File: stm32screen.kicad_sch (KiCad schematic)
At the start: 31 parts, among them J1 SWD, J2 GC9A01, J3 Oil temp sensor, J4 pressure sensor, J5 POWER IN, SW1 SW_Push, SW2 SW_Push, U1 TS1117BCW-3.3, U2 STM32F407VETx

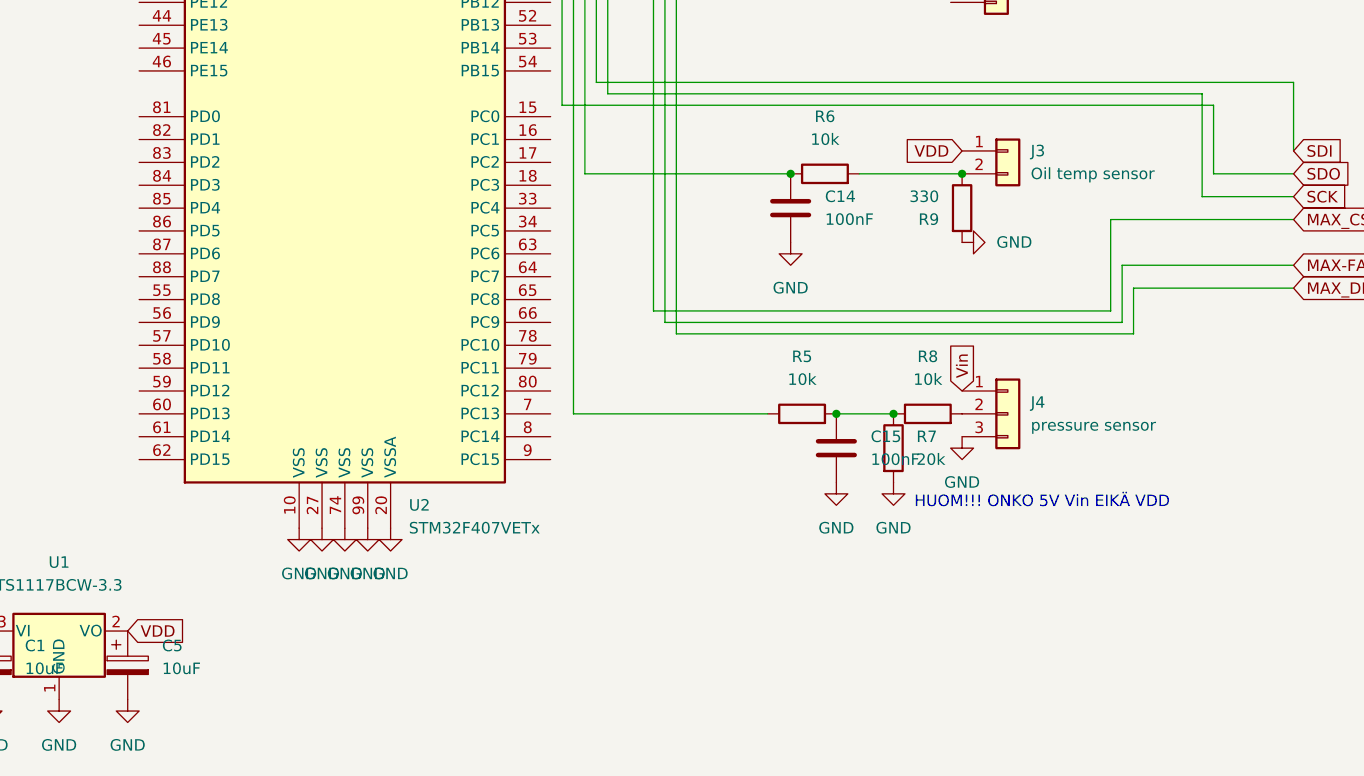
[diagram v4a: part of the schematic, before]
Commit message: THT caps to MLCC as per TS1117B datasheet. STM32 ref caps as well
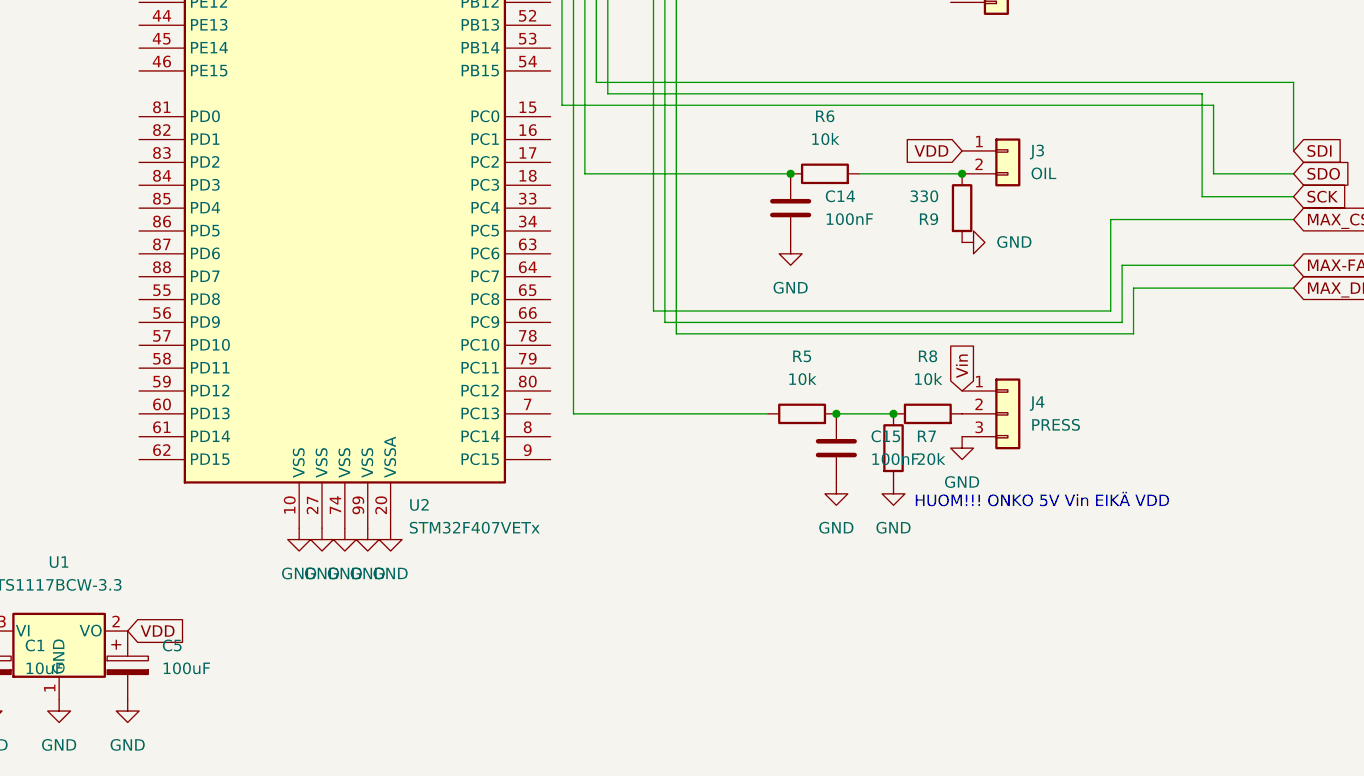
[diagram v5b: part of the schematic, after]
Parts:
- C1: footprint Capacitor_THT:CP_Radial_D5.0mm_P2.00mm -> Capacitor_SMD:C_1210_3225Metric_Pad1.33x2.70mm_HandSolder
- C2, C3: footprint Capacitor_THT:CP_Radial_D5.0mm_P2.00mm -> Capacitor_SMD:C_1206_3216Metric_Pad1.33x1.80mm_HandSolder
- C5: value 10uF -> 100uF; footprint Capacitor_THT:CP_Radial_D5.0mm_P2.00mm -> Capacitor_SMD:C_1210_3225Metric_Pad1.33x2.70mm_HandSolder
- J3: value Oil temp sensor -> OIL
- J4: value pressure sensor -> PRESS
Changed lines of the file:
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@@
 			)
 		)
-		(property "Footprint" "Capacitor_THT:CP_Radial_D5.0mm_P2.00mm"
+		(property "Footprint" "Capacitor_SMD:C_1206_3216Metric_Pad1.33x1.80mm_HandSolder"
 			(at 34.29 47.9552 0)
 			(effects
@@
 			)
 		)
-		(property "Footprint" "Capacitor_THT:CP_Radial_D5.0mm_P2.00mm"
+		(property "Footprint" "Capacitor_SMD:C_1206_3216Metric_Pad1.33x1.80mm_HandSolder"
 			(at 34.29 45.4152 0)
 			(effects
@@
 			)
 		)
-		(property "Value" "pressure sensor"
+		(property "Value" "PRESS"
 			(at 140.97 154.9399 0)
 			(effects
@@
 			)
 		)
-		(property "Value" "Oil temp sensor"
+		(property "Value" "OIL"
 			(at 140.97 126.9999 0)
 			(effects
@@
 			)
 		)
-		(property "Footprint" "Capacitor_THT:CP_Radial_D5.0mm_P2.00mm"
+		(property "Footprint" "Capacitor_SMD:C_1210_3225Metric_Pad1.33x2.70mm_HandSolder"
 			(at 26.3652 185.42 0)
 			(effects
@@
 			)
 		)
-		(property "Value" "10uF"
+		(property "Value" "100uF"
 			(at 44.45 181.9909 0)
 			(effects
@@
 			)
 		)
-		(property "Footprint" "Capacitor_THT:CP_Radial_D5.0mm_P2.00mm"
+		(property "Footprint" "Capacitor_SMD:C_1210_3225Metric_Pad1.33x2.70mm_HandSolder"
 			(at 41.6052 185.42 0)
 			(effects

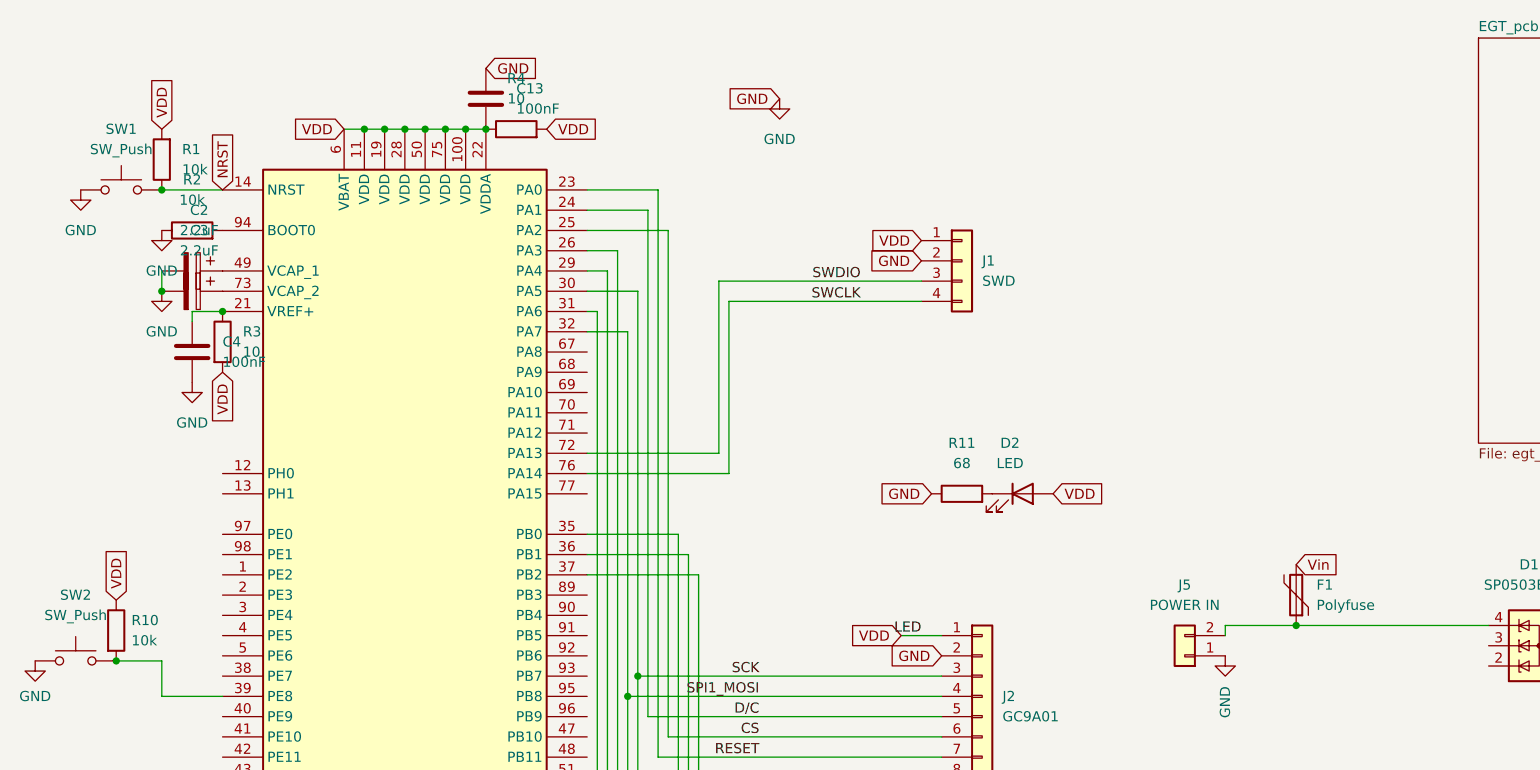
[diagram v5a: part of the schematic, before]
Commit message: Adjusted silkscreen and component layout, changed some component values so that silkscreen doesn't change every time
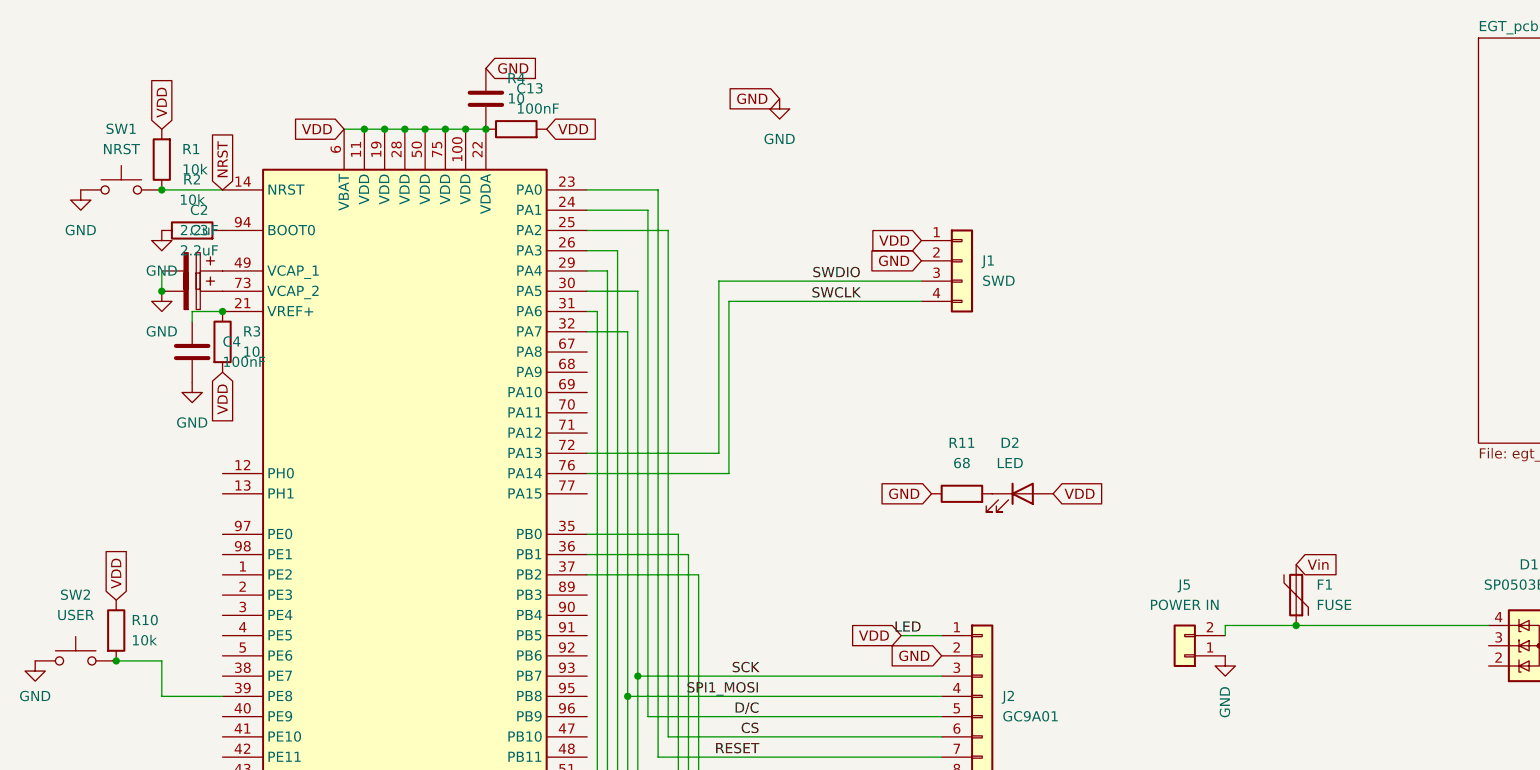
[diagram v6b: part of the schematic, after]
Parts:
- F1: value Polyfuse -> FUSE
- SW1: value SW_Push -> NRST
- SW2: value SW_Push -> USER
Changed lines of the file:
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@@
 			)
 		)
-		(property "Value" "SW_Push"
+		(property "Value" "NRST"
 			(at 29.21 29.21 0)
 			(effects
@@
 			)
 		)
-		(property "Value" "Polyfuse"
+		(property "Value" "FUSE"
 			(at 179.07 86.3599 0)
 			(effects
@@
 			)
 		)
-		(property "Value" "SW_Push"
+		(property "Value" "USER"
 			(at 23.495 87.63 0)
 			(effects

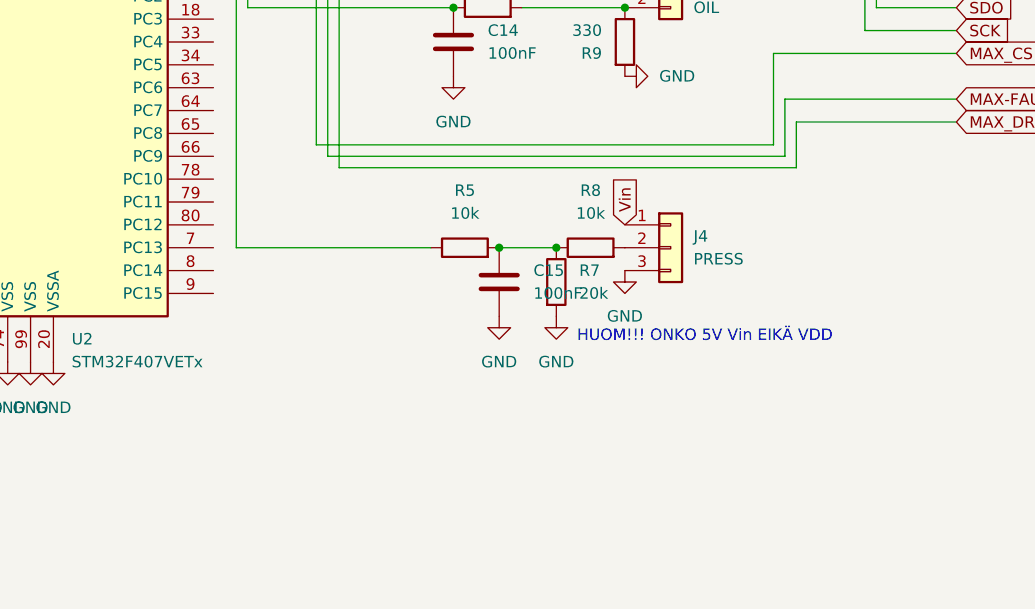
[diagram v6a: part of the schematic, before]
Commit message: Add voltage divider for 5v if using 12v in
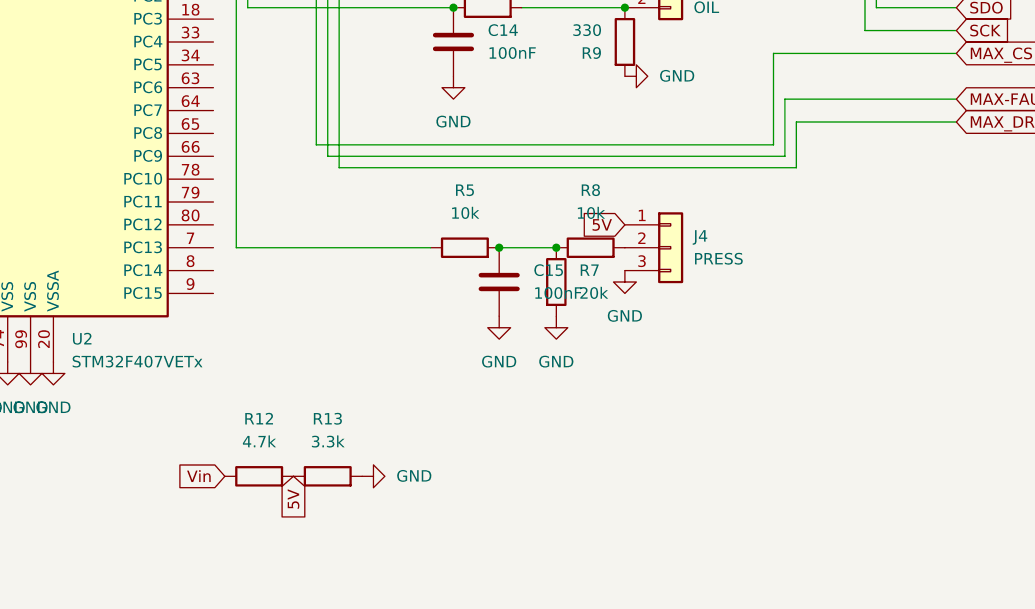
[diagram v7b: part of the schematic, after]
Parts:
- added R12: 4.7k, Resistor_SMD:R_0201_0603Metric_Pad0.64x0.40mm_HandSolder, symbol Device:R
- added R13: 3.3k, Resistor_SMD:R_0805_2012Metric_Pad1.20x1.40mm_HandSolder, symbol Device:R
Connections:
- net GND: now also R13.2
- net Vin: now also R12.1; no longer J4.1 (Pin_1)
- new net 5V: J4.1 (Pin_1), R12.2, R13.1
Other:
- note removed: "HUOM!!! ONKO 5V Vin EIKÄ VDD"

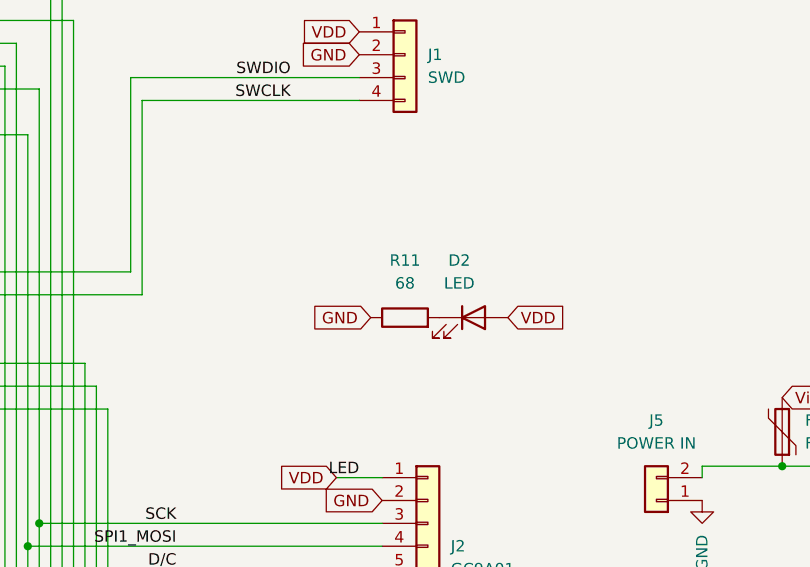
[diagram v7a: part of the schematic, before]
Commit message: Changed footprints to larger ones and for general unity of footprints
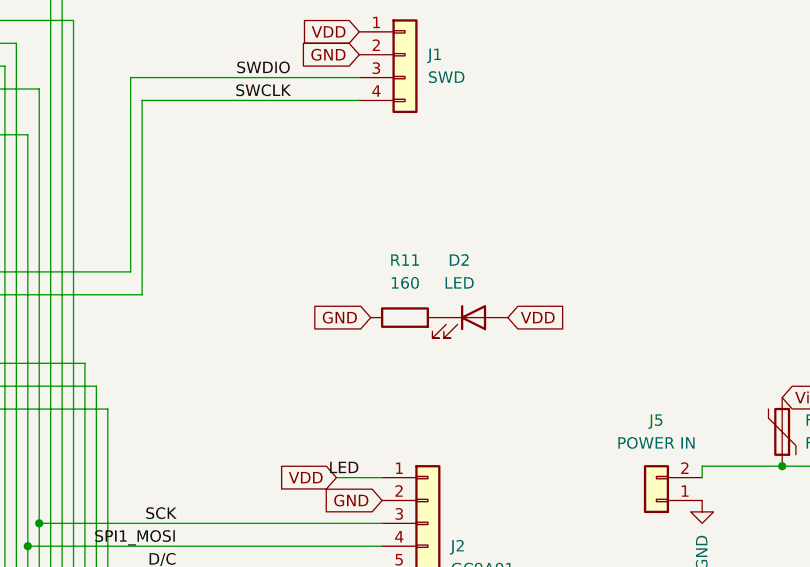
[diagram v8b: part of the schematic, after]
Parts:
- R11: value 68 -> 160
- R12: footprint Resistor_SMD:R_0201_0603Metric_Pad0.64x0.40mm_HandSolder -> Resistor_SMD:R_0805_2012Metric_Pad1.20x1.40mm_HandSolder
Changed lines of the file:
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@@
 			)
 		)
-		(property "Value" "68"
+		(property "Value" "160"
 			(at 134.62 68.58 90)
 			(effects
@@
 			)
 		)
-		(property "Footprint" "Resistor_SMD:R_0201_0603Metric_Pad0.64x0.40mm_HandSolder"
+		(property "Footprint" "Resistor_SMD:R_0805_2012Metric_Pad1.20x1.40mm_HandSolder"
 			(at 92.71 180.848 90)
 			(effects
